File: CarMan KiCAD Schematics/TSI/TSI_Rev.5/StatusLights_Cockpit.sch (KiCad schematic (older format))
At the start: 20 parts, among them Q3 ZVP1320F, U1 RDE03110S12, U11 TLP293, U13 TLP293, U27 TLP293

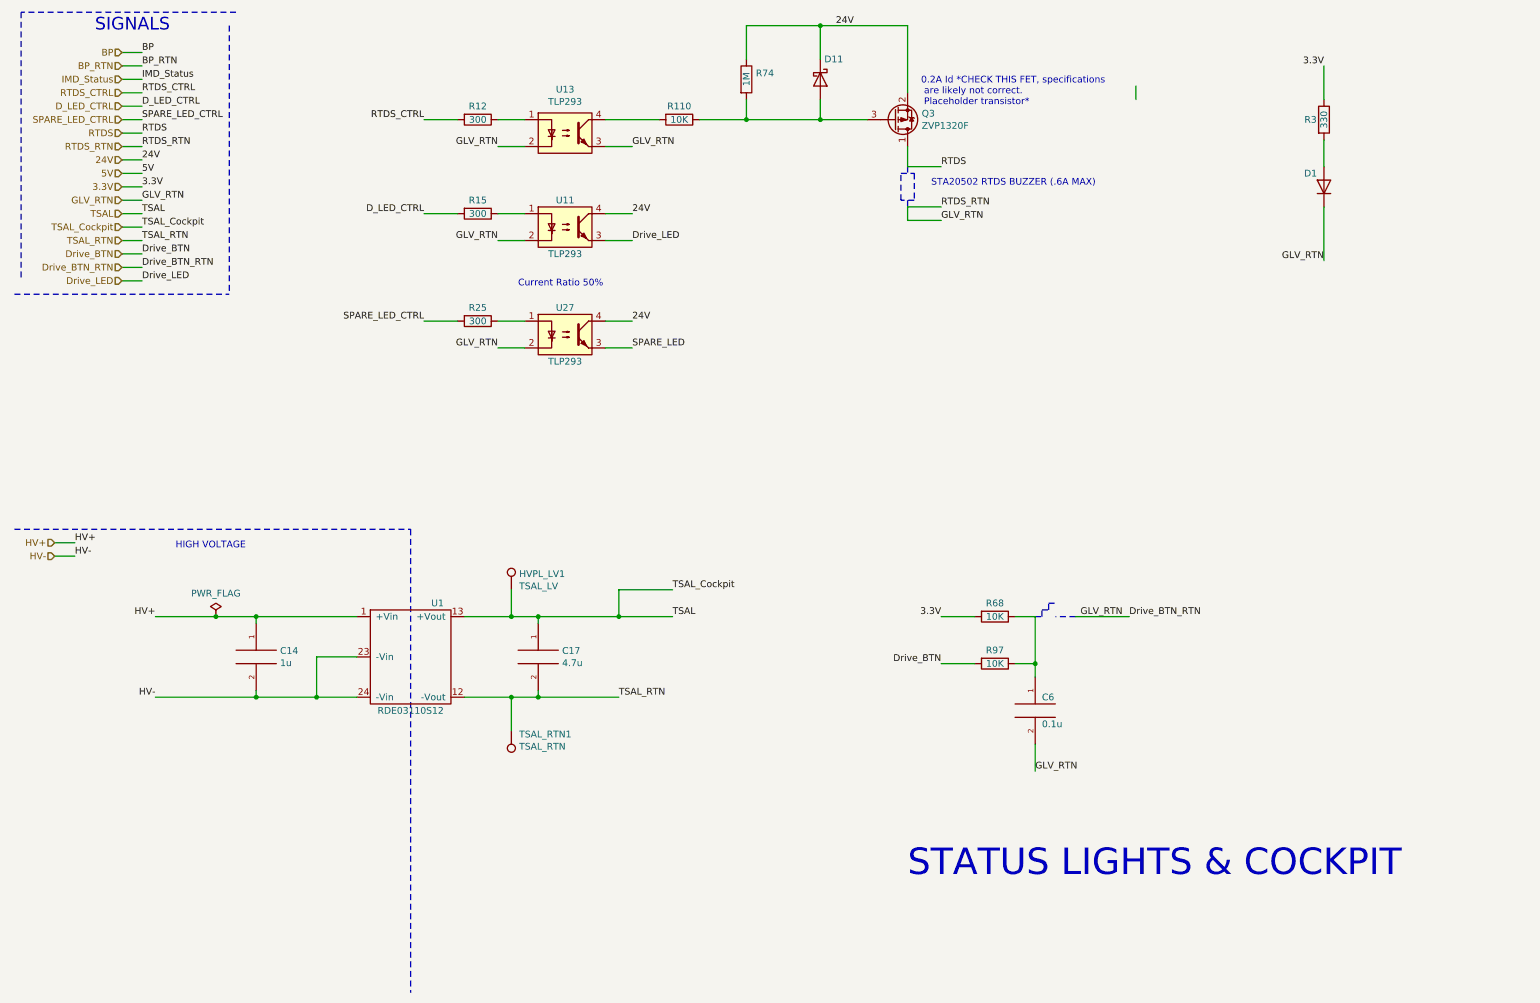
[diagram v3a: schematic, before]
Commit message: footprinting, datasheeting, general bug fixes * Added TSAL & TSAL Cockpit labels
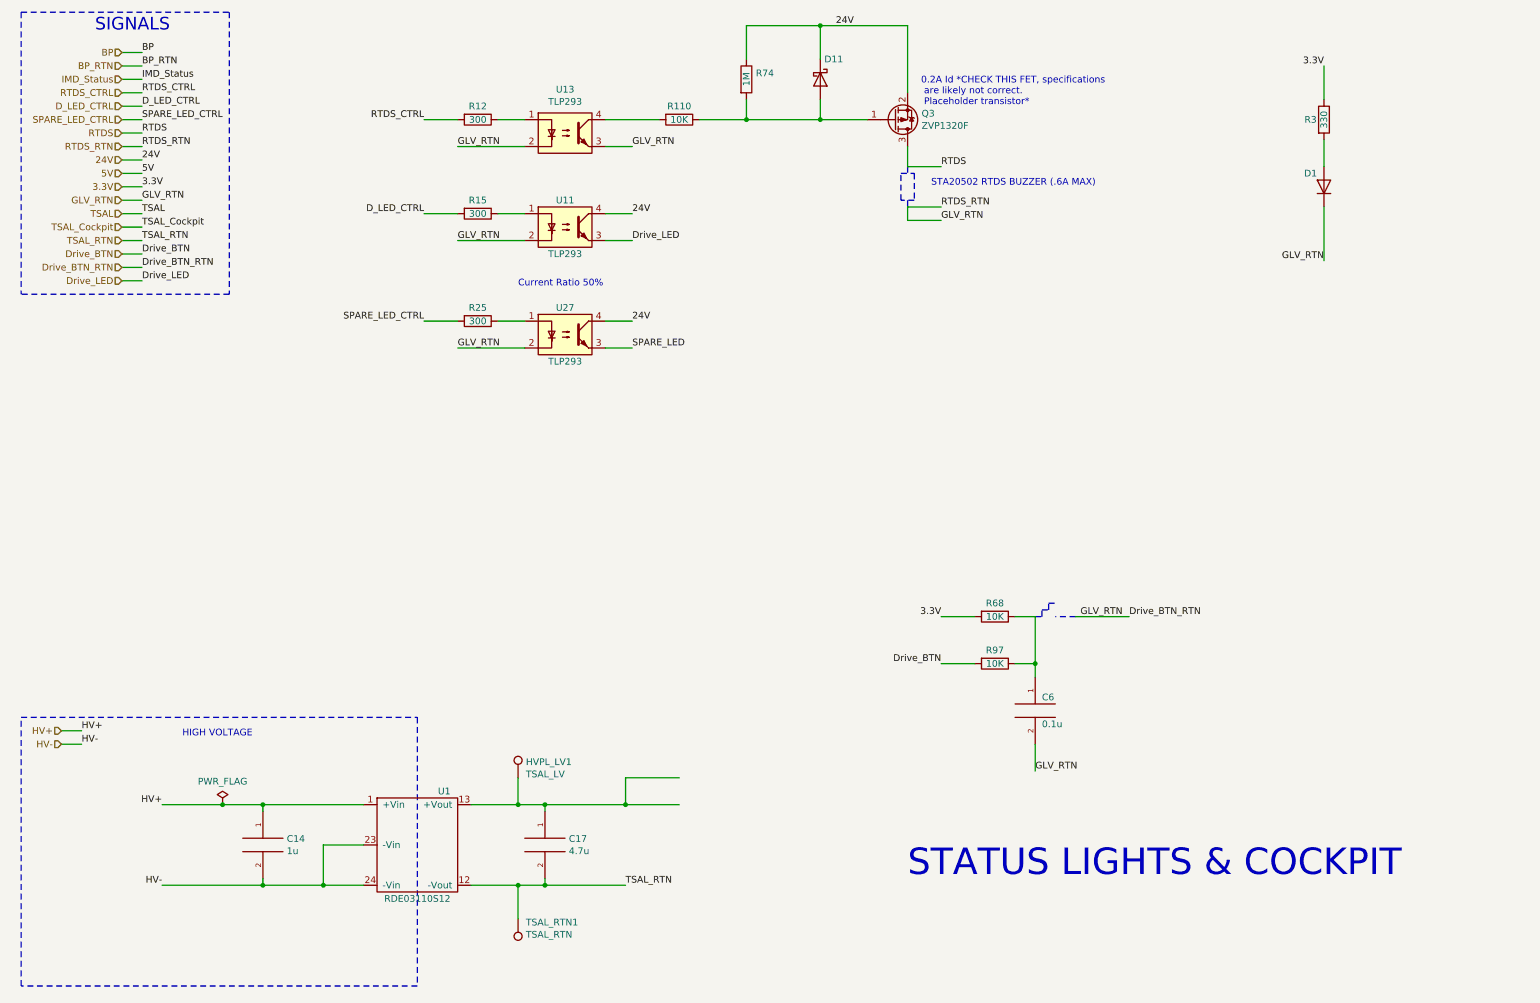
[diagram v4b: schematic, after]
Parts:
- removed Q3: ZVP1320F, symbol Device:Q_PMOS_DSG
- added Q3: ZVP1320F, TSI_Rev_2021_Footprint_Lib:SOT23, symbol Device:Q_PMOS_GSD
- U1: footprint (none) -> TSI_Rev_2021_Footprint_Lib:DIP1549W45P254L3404H940Q24
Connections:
- wire segments 85 -> 84
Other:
- moved on the sheet: C14, C17, HVPL_LV1, TSAL_RTN1, U1
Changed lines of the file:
@@
 	10200 1950 10200 2350
-Wire Wire Line
-	8800 1050 8800 1150
 Wire Wire Line
 	10200 1150 10200 900
@@
 Text Label 3500 1300 2    50   ~ 0
 RTDS_CTRL
-Text Label 4050 1500 2    50   ~ 0
+Text Label 3750 1500 0    50   ~ 0
 GLV_RTN
 $Comp
@@
 Text Label 5050 2200 0    50   ~ 0
 Drive_LED
-Text Label 4050 2200 2    50   ~ 0
+Text Label 3750 2200 0    50   ~ 0
 GLV_RTN
 Text Label 3500 2000 2    50   ~ 0
@@
 Wire Wire Line
 	3750 2800 3500 2800
-Text Label 4050 3000 2    50   ~ 0
+Text Label 3750 3000 0    50   ~ 0
 GLV_RTN
 Text Label 5050 3000 0    50   ~ 0
@@
 Text Label 3500 2800 2    50   ~ 0
 SPARE_LED_CTRL
-$Comp
-L Device:Q_PMOS_DSG Q3
-U 1 1 5FA04A44
-P 7000 1300
-F 0 "Q3" H 7205 1254 50  0000 L CNN
-F 1 "ZVP1320F" H 7205 1345 50  0000 L CNN
-F 2 "" H 7200 1400 50  0001 C CNN
-F 3 "~" H 7000 1300 50  0001 C CNN
-	1    7000 1300
-	1    0    0    1
-$EndComp
 Wire Wire Line
 	7100 600  7100 1100
@@
 Text Notes 8500 1800 2    50   ~ 0
 STA20502 RTDS BUZZER (.6A MAX)\n
-Wire Notes Line
-	450  4350 3400 4350
-Wire Notes Line
-	3400 4350 3400 7800
-Text HLabel 750  4450 0    50   Input ~ 0
+Text HLabel 800  5850 0    50   Input ~ 0
 HV+
-Text HLabel 750  4550 0    50   Input ~ 0
+Text HLabel 800  5950 0    50   Input ~ 0
 HV-
 Wire Wire Line
-	750  4450 900  4450
-Wire Wire Line
-	750  4550 900  4550
-Text Label 900  4450 0    50   ~ 0
+	800  5850 950  5850
+Wire Wire Line
+	800  5950 950  5950
+Text Label 950  5850 0    50   ~ 0
 HV+
-Text Label 900  4550 0    50   ~ 0
+Text Label 950  5950 0    50   ~ 0
 HV-
 Wire Wire Line
-	3000 5300 2700 5300
-Wire Wire Line
-	1500 5000 1950 5000
+	3050 6700 2750 6700
+Wire Wire Line
+	1550 6400 2000 6400
 $Comp
 L CarMan_KiCAD_Library:RDE03110S12 U1
 U 1 1 5FA31407
-P 3400 5300
-F 0 "U1" H 3600 5700 50  0000 C CNN
-F 1 "RDE03110S12" H 3400 4900 50  0000 C CNN
-F 2 "" H 3200 5450 50  0001 C CNN
-F 3 "" H 3200 5450 50  0001 C CNN
-	1    3400 5300
-	1    0    0    -1
-$EndComp
-Wire Wire Line
-	1500 5600 2250 5600
-Wire Wire Line
-	2700 5300 2700 5600
-Connection ~ 2700 5600
-Wire Wire Line
-	2700 5600 3000 5600
+P 3450 6700
+F 0 "U1" H 3650 7100 50  0000 C CNN
+F 1 "RDE03110S12" H 3450 6300 50  0000 C CNN
+F 2 "TSI_Rev_2021_Footprint_Lib:DIP1549W45P254L3404H940Q24" H 3250 6850 50  0001 C CNN
+F 3 "https://www.snapeda.com/parts/RDE03110S12/XP%20Power/datasheet/" H 3250 6850 50  0001 C CNN
+	1    3450 6700
+	1    0    0    -1
+$EndComp
+Wire Wire Line
+	1550 7000 2300 7000
+Wire Wire Line
+	2750 6700 2750 7000
+Connection ~ 2750 7000
+Wire Wire Line
+	2750 7000 3050 7000
 $Comp
 L pspice:CAP C14
 U 1 1 5FA3C7FB
-P 2250 5300
-F 0 "C14" H 2428 5346 50  0000 L CNN
-F 1 "1u" H 2428 5255 50  0000 L CNN
-F 2 "" H 2250 5300 50  0001 C CNN
-F 3 "~" H 2250 5300 50  0001 C CNN
-	1    2250 5300
-	1    0    0    -1
-$EndComp
-Wire Wire Line
-	2250 5550 2250 5600
-Connection ~ 2250 5600
-Wire Wire Line
-	2250 5600 2700 5600
-Wire Wire Line
-	2250 5050 2250 5000
-Connection ~ 2250 5000
-Wire Wire Line
-	2250 5000 3000 5000
+P 2300 6700
+F 0 "C14" H 2478 6746 50  0000 L CNN
+F 1 "1u" H 2478 6655 50  0000 L CNN
+F 2 "" H 2300 6700 50  0001 C CNN
+F 3 "~" H 2300 6700 50  0001 C CNN
+	1    2300 6700
+	1    0    0    -1
+$EndComp
+Wire Wire Line
+	2300 6950 2300 7000
+Connection ~ 2300 7000
+Wire Wire Line
+	2300 7000 2750 7000
+Wire Wire Line
+	2300 6450 2300 6400
+Connection ~ 2300 6400
+Wire Wire Line
+	2300 6400 3050 6400
 $Comp
 L power:PWR_FLAG #FLG01
 U 1 1 5FA42854
-P 1950 5000
-F 0 "#FLG01" H 1950 5075 50  0001 C CNN
-F 1 "PWR_FLAG" H 1950 5173 50  0000 C CNN
-F 2 "" H 1950 5000 50  0001 C CNN
-F 3 "~" H 1950 5000 50  0001 C CNN
-	1    1950 5000
-	1    0    0    -1
-$EndComp
-Connection ~ 1950 5000
-Wire Wire Line
-	1950 5000 2250 5000
-Text Label 1500 5000 2    50   ~ 0
+P 2000 6400
+F 0 "#FLG01" H 2000 6475 50  0001 C CNN
+F 1 "PWR_FLAG" H 2000 6573 50  0000 C CNN
+F 2 "" H 2000 6400 50  0001 C CNN
+F 3 "~" H 2000 6400 50  0001 C CNN
+	1    2000 6400
+	1    0    0    -1
+$EndComp
+Connection ~ 2000 6400
+Wire Wire Line
+	2000 6400 2300 6400
+Text Label 1550 6400 2    50   ~ 0
 HV+
-Text Label 1500 5600 2    50   ~ 0
+Text Label 1550 7000 2    50   ~ 0
 HV-
 Wire Wire Line
-	3800 5600 4150 5600
-Wire Wire Line
-	3800 5000 4150 5000
-Wire Wire Line
-	4950 5000 4950 4800
-Wire Wire Line
-	4950 4800 5350 4800
-Connection ~ 4950 5000
-Wire Wire Line
-	4950 5000 5350 5000
+	3850 7000 4200 7000
+Wire Wire Line
+	3850 6400 4200 6400
+Wire Wire Line
+	5000 6400 5000 6200
+Wire Wire Line
+	5000 6200 5400 6200
+Connection ~ 5000 6400
+Wire Wire Line
+	5000 6400 5400 6400
 $Comp
 L pspice:CAP C17
 U 1 1 5FA50112
-P 4350 5300
-F 0 "C17" H 4528 5346 50  0000 L CNN
-F 1 "4.7u" H 4528 5255 50  0000 L CNN
-F 2 "" H 4350 5300 50  0001 C CNN
-F 3 "~" H 4350 5300 50  0001 C CNN
-	1    4350 5300
-	1    0    0    -1
-$EndComp
-Wire Wire Line
-	4350 5050 4350 5000
-Connection ~ 4350 5000
-Wire Wire Line
-	4350 5000 4950 5000
-Wire Wire Line
-	4350 5550 4350 5600
-Connection ~ 4350 5600
-Wire Wire Line
-	4350 5600 4950 5600
-Wire Wire Line
-	4150 5000 4150 4800
-Connection ~ 4150 5000
-Wire Wire Line
-	4150 5000 4350 5000
-Wire Wire Line
-	4150 5600 4150 5850
-Connection ~ 4150 5600
-Wire Wire Line
-	4150 5600 4350 5600
-Text Label 4950 5600 0    50   ~ 0
+P 4400 6700
+F 0 "C17" H 4578 6746 50  0000 L CNN
+F 1 "4.7u" H 4578 6655 50  0000 L CNN
+F 2 "" H 4400 6700 50  0001 C CNN
+F 3 "~" H 4400 6700 50  0001 C CNN
+	1    4400 6700
+	1    0    0    -1
+$EndComp
+Wire Wire Line
+	4400 6450 4400 6400
+Connection ~ 4400 6400
+Wire Wire Line
+	4400 6400 5000 6400
+Wire Wire Line
+	4400 6950 4400 7000
+Connection ~ 4400 7000
+Wire Wire Line
+	4400 7000 5000 7000
+Wire Wire Line
+	4200 6400 4200 6200
+Connection ~ 4200 6400
+Wire Wire Line
+	4200 6400 4400 6400
+Wire Wire Line
+	4200 7000 4200 7250
+Connection ~ 4200 7000
+Wire Wire Line
+	4200 7000 4400 7000
+Text Label 5000 7000 0    50   ~ 0
 TSAL_RTN
-Text Label 5350 5000 0    50   ~ 0
-TSAL
-Text Label 5350 4800 0    50   ~ 0
-TSAL_Cockpit
 Text Notes 7200 1200 0    50   ~ 0
 0.2A Id *CHECK THIS FET, specifications\n are likely not correct.\n Placeholder transistor*
@@
 L Connector:TestPoint HVPL_LV1
 U 1 1 5FA80FFC
-P 4150 4800
-F 0 "HVPL_LV1" H 4208 4918 50  0000 L CNN
-F 1 "TSAL_LV" H 4208 4827 50  0000 L CNN
-F 2 "" H 4350 4800 50  0001 C CNN
-F 3 "~" H 4350 4800 50  0001 C CNN
-	1    4150 4800
+P 4200 6200
+F 0 "HVPL_LV1" H 4258 6318 50  0000 L CNN
+F 1 "TSAL_LV" H 4258 6227 50  0000 L CNN
+F 2 "" H 4400 6200 50  0001 C CNN
+F 3 "~" H 4400 6200 50  0001 C CNN
+	1    4200 6200
 	1    0    0    -1
 $EndComp
@@
 L Connector:TestPoint TSAL_RTN1
 U 1 1 5FA8198D
-P 4150 5850
-F 0 "TSAL_RTN1" H 4092 5876 50  0000 R CNN
-F 1 "TSAL_RTN" H 4092 5967 50  0000 R CNN
-F 2 "" H 4350 5850 50  0001 C CNN
-F 3 "~" H 4350 5850 50  0001 C CNN
-	1    4150 5850
+P 4200 7250
+F 0 "TSAL_RTN1" H 4142 7276 50  0000 R CNN
+F 1 "TSAL_RTN" H 4142 7367 50  0000 R CNN
+F 2 "" H 4400 7250 50  0001 C CNN
+F 3 "~" H 4400 7250 50  0001 C CNN
+	1    4200 7250
 	-1   0    0    1
 $EndComp
-Text Notes 1650 4500 0    50   ~ 0
+Text Notes 1700 5900 0    50   ~ 0
 HIGH VOLTAGE\n
 $Comp
@@
 	4250 2800 4050 2800
 Wire Wire Line
-	4250 3000 4050 3000
-Wire Wire Line
 	5050 2000 4850 2000
 Wire Wire Line
 	5050 2200 4850 2200
 Wire Wire Line
-	4250 2200 4050 2200
-Wire Wire Line
 	4250 2000 4050 2000
 Wire Wire Line
 	4250 1300 4050 1300
-Wire Wire Line
-	4250 1500 4050 1500
 Wire Wire Line
 	5050 1500 4850 1500
@@
 Wire Wire Line
 	1250 1500 1400 1500
-Wire Notes Line
-	2100 500  500  500
-Wire Notes Line
-	450  2600 2050 2600
-Wire Notes Line
-	2050 600  2050 2600
-Wire Notes Line
-	500  500  500  2500
 Text Notes 1050 650  0    94   ~ 0
 SIGNALS\n
@@
 Text Label 1400 2500 0    50   ~ 0
 Drive_LED
+Wire Notes Line
+	2050 500  2050 2600
+Wire Notes Line
+	500  500  2050 500
+Wire Notes Line
+	2050 2600 500  2600
+Wire Notes Line
+	500  500  500  2600
+Wire Wire Line
+	3750 3000 4250 3000
+Wire Wire Line
+	3750 2200 4250 2200
+Wire Wire Line
+	3750 1500 4250 1500
+$Comp
+L Device:Q_PMOS_GSD Q?
+U 1 1 5FC93215
+P 7000 1300
+AR Path="/6196BF15/5FC93215" Ref="Q?"  Part="1"
+AR Path="/5FE1DCBA/5FC93215" Ref="Q3"  Part="1"
+F 0 "Q3" H 7204 1254 50  0000 L CNN
+F 1 "ZVP1320F" H 7204 1345 50  0000 L CNN
+F 2 "TSI_Rev_2021_Footprint_Lib:SOT23" H 7200 1400 50  0001 C CNN
+F 3 "https://www.snapeda.com/parts/ZVP1320FTA/Diodes%20Inc./datasheet/" H 7000 1300 50  0001 C CNN
+	1    7000 1300
+	1    0    0    1
+$EndComp
+Wire Notes Line
+	3450 5750 3450 7750
+Wire Notes Line
+	3450 7750 500  7750
+Wire Notes Line
+	500  7750 500  5750
+Wire Notes Line
+	500  5750 3450 5750
 $EndSCHEMATC

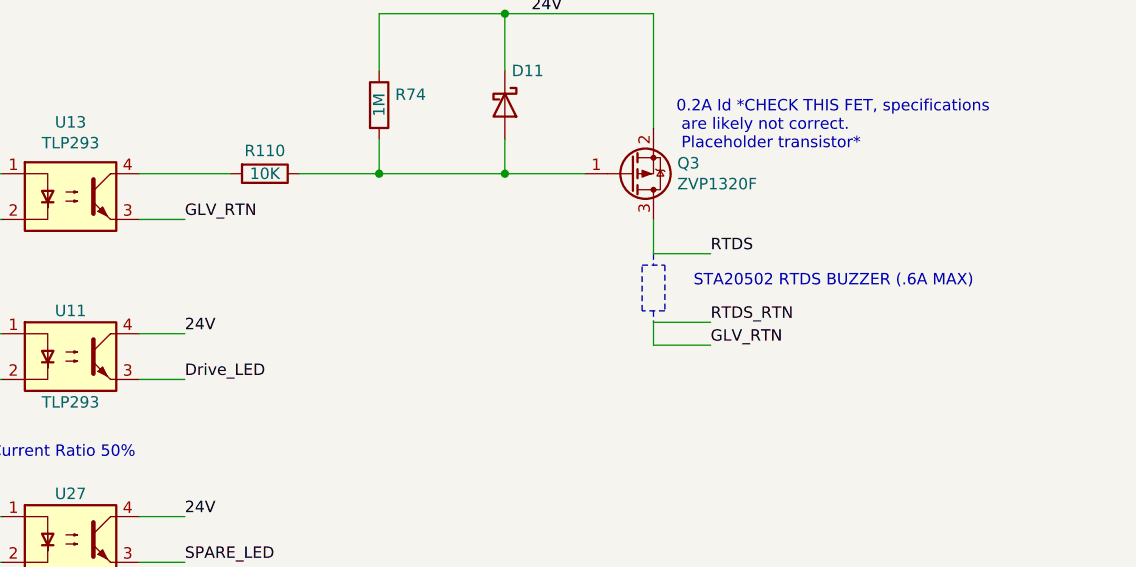
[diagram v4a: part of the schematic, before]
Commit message: - TSI editing, Xsistor selection, footprints
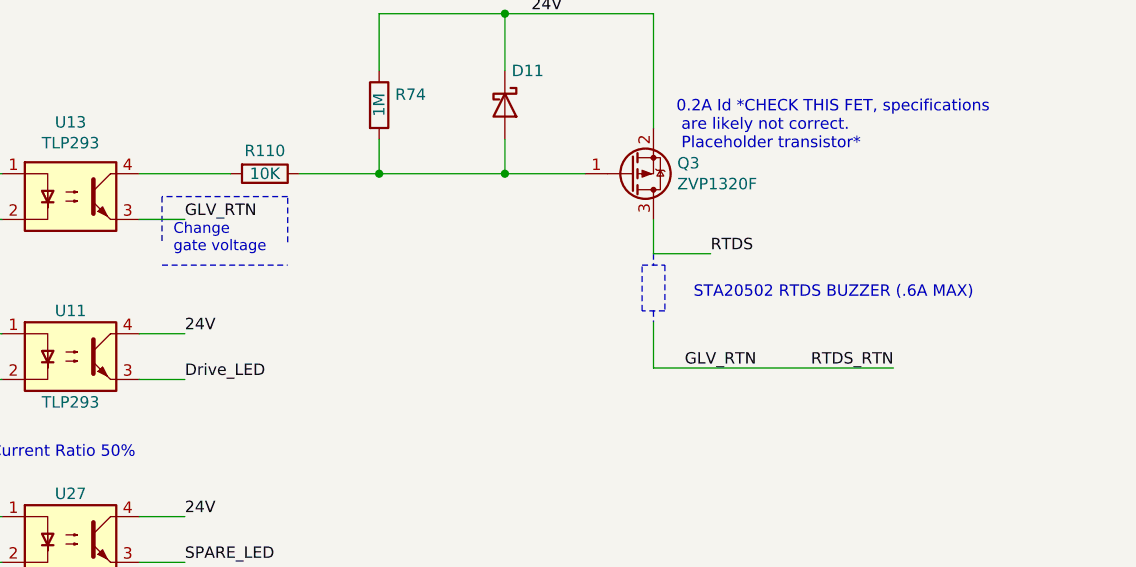
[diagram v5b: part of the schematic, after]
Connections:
- wire segments 84 -> 83
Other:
- note added: "Change \ngate voltage\n"
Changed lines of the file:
@@
-$EndComp
-$Comp
-L CarMan_KiCAD_Library:D_Schottky D11
-U 1 1 5F9B6857
-P 6450 1000
-F 0 "D11" V 6300 1100 50  0000 C CNN
-F 1 "D_Schottky" H 6450 1126 50  0001 C CNN
-F 2 "" H 6450 1000 50  0001 C CNN
-F 3 "~" H 6450 1000 50  0001 C CNN
-	1    6450 1000
-	0    1    1    0
 $EndComp
 $Comp
@@
 Wire Wire Line
 	7100 600  7100 1100
-Wire Wire Line
-	6450 1300 6800 1300
 Connection ~ 6450 1300
 Wire Wire Line
@@
 Text Label 6700 600  2    50   ~ 0
 24V
-Wire Wire Line
-	7100 1950 7100 2050
-Wire Wire Line
-	7100 2050 7350 2050
-Wire Wire Line
-	7100 1950 7350 1950
-Text Label 7350 1950 0    50   ~ 0
+Text Label 8150 2150 2    50   ~ 0
 RTDS_RTN
-Text Label 7350 2050 0    50   ~ 0
+Text Label 7550 2150 2    50   ~ 0
 GLV_RTN
 Wire Notes Line
@@
 Wire Notes Line
 	7100 1900 7100 1950
-Text Notes 8500 1800 2    50   ~ 0
+Text Notes 8500 1850 2    50   ~ 0
 STA20502 RTDS BUZZER (.6A MAX)\n
 Text HLabel 800  5850 0    50   Input ~ 0
@@
 Wire Notes Line
 	500  5750 3450 5750
+Wire Wire Line
+	6450 1300 6800 1300
+Wire Wire Line
+	7100 2150 8150 2150
+Wire Wire Line
+	7100 1950 7100 2150
+$Comp
+L CarMan_KiCAD_Library:D_Schottky D11
+U 1 1 5F9B6857
+P 6450 1000
+F 0 "D11" V 6300 1100 50  0000 C CNN
+F 1 "D_Schottky" H 6450 1126 50  0001 C CNN
+F 2 "" H 6450 1000 50  0001 C CNN
+F 3 "~" H 6450 1000 50  0001 C CNN
+	1    6450 1000
+	0    1    1    0
+$EndComp
+Text Notes 5000 1650 0    47   ~ 0
+Change \ngate voltage\n
+Wire Notes Line
+	4950 1700 5500 1700
+Wire Notes Line
+	5500 1600 5500 1400
+Wire Notes Line
+	5500 1400 4950 1400
+Wire Notes Line
+	4950 1400 4950 1600
 $EndSCHEMATC

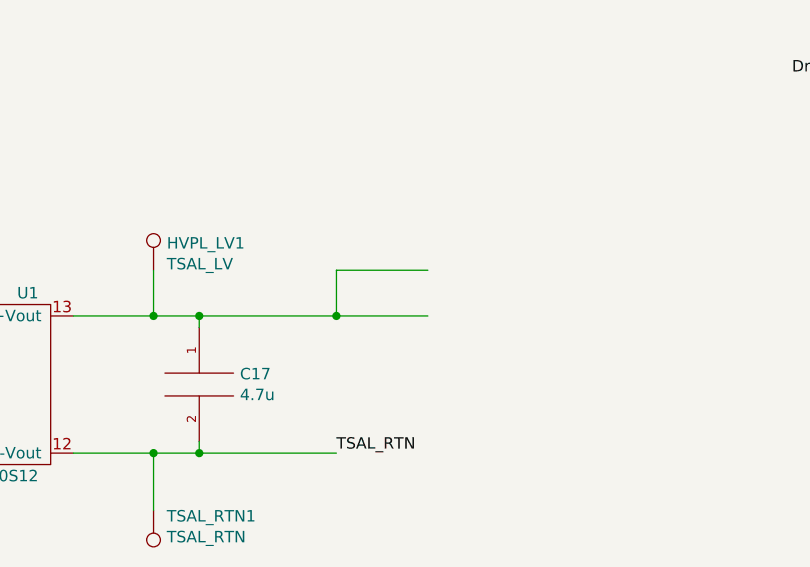
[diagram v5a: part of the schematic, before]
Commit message: - Aesthetics - TSI Safety Loop Edits - Battery pack connection editing
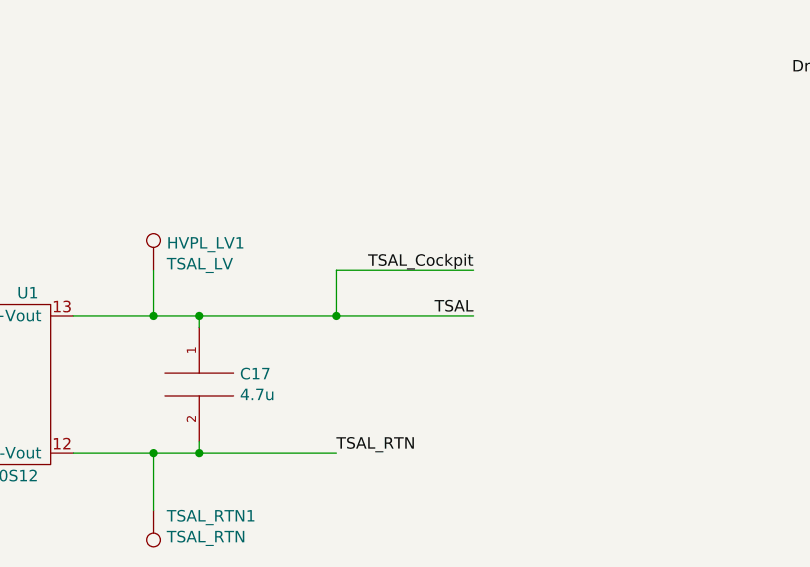
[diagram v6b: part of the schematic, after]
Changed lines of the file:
@@
 $Descr A4 11693 8268
 encoding utf-8
-Sheet 6 6
+Sheet 4 6
 Title ""
 Date ""
@@
 Wire Wire Line
 	5000 6400 5000 6200
-Wire Wire Line
-	5000 6200 5400 6200
 Connection ~ 5000 6400
-Wire Wire Line
-	5000 6400 5400 6400
 $Comp
 L pspice:CAP C17
@@
 Wire Notes Line
 	4950 1400 4950 1600
+Text Label 5600 6400 2    50   ~ 0
+TSAL
+Text Label 5600 6200 2    50   ~ 0
+TSAL_Cockpit
+Wire Wire Line
+	5000 6200 5600 6200
+Wire Wire Line
+	5000 6400 5600 6400
 $EndSCHEMATC
